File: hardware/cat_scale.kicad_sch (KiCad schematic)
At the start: 40 parts, among them J1 USB_C_Receptacle_USB2.0, J2 UART, J3 I2C, J4 LOAD CELL, J5 SSD1306, Q1 S8550, SW1 RST, SW2 BOOT, SW3 RotaryEncoder_Switch, U1 ESP32-S2-SOLO-U-N4R2, U2 AMS1117-3.3, U3 HX711

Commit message: Fixed PCB design
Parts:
- removed Q1: S8550, Package_TO_SOT_SMD:SOT-23, symbol Transistor_BJT:S8550
- added J6: Conn_01x02_Pin, Connector_PinHeader_2.54mm:PinHeader_1x02_P2.54mm_Vertical, symbol Connector:Conn_01x02_Pin
- added Q2: MMBT4403, Package_TO_SOT_SMD:SOT-23, symbol Transistor_BJT:MMBT3906
- added R11, R12: 10k, Resistor_SMD:R_1206_3216Metric, symbol Device:R
- C8: value 1uF -> 10uF
- C9: value 1uF -> 0.1uF
- D1: value LED -> PWR
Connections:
- net +3V3: now also Q2.2 (E), R11.2, R12.2; no longer J5.1 (Pin_1)
- net AVDD: now also Q2.3 (C)
- net GND: now also J6.2 (Pin_2)
- net SCL: now also J3.3 (Pin_3), J5.3 (Pin_3), U1.34 (IO41), R11.1; no longer J3.4 (Pin_4), J5.4 (Pin_4), U1.24 (IO33)
- net SDA: now also J3.4 (Pin_4), J5.4 (Pin_4), U1.35 (IO42), R12.1; no longer J3.3 (Pin_3), J5.3 (Pin_3), U1.25 (IO34)
- net +5V: now reaches C5.2, D2.1 (K), U2.3 (VI)
- net +5V: now also J5.1 (Pin_1), J6.1 (Pin_1)
- net at U3.2 (BASE): now also Q2.1 (B)
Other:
- moved on the sheet: C10, C7, C8, C9, H1, H2, H3, H4, J4, J5, R7, R8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

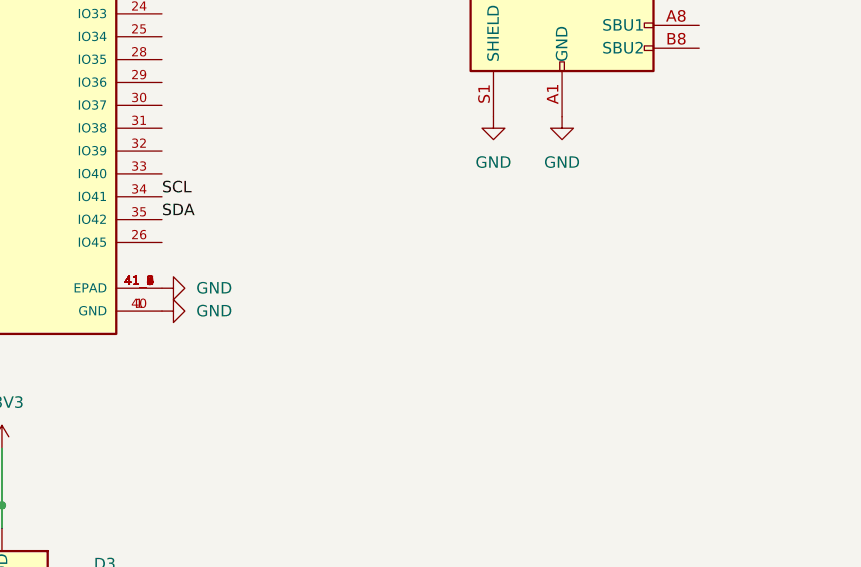
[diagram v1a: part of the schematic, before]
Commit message: * PCB: Added buzzer
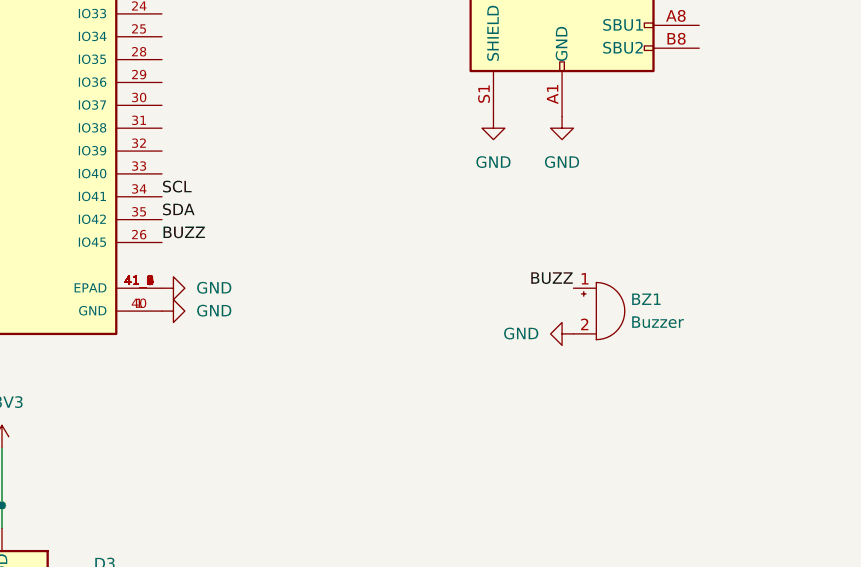
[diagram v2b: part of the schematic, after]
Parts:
- added BZ1: Buzzer, Buzzer_Beeper:Buzzer_Murata_PKMCS0909E, symbol Device:Buzzer
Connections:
- net GND: now also BZ1.2 (+)
- net BUZZ: now reaches U1.26 (IO45)
- net BUZZ: now also BZ1.1 (-)
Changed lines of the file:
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@@
+    (effects (font (size 1.27 1.27)) (justify right bottom))
+  )
+  (label "BUZZ" (at 199.39 121.92 180) (fields_autoplaced)
     (effects (font (size 1.27 1.27)) (justify right bottom))
   )
@@
   )
   (label "HX711_DATA" (at 92.71 158.75 0) (fields_autoplaced)
+    (effects (font (size 1.27 1.27)) (justify left bottom))
+  )
+  (label "BUZZ" (at 153.67 116.84 0) (fields_autoplaced)
     (effects (font (size 1.27 1.27)) (justify left bottom))
   )
@@
     )
   )
+  (symbol (lib_id "Device:Buzzer") (at 201.93 124.46 0) (unit 1)
+    (in_bom yes) (on_board yes) (dnp no) (fields_autoplaced)
+    (property "Reference" "BZ1" (at 205.74 123.19 0)
+      (effects (font (size 1.27 1.27)) (justify left))
+    )
+    (property "Value" "Buzzer" (at 205.74 125.73 0)
+      (effects (font (size 1.27 1.27)) (justify left))
+    )
+    (property "Footprint" "Buzzer_Beeper:Buzzer_Murata_PKMCS0909E" (at 201.295 121.92 90)
+      (effects (font (size 1.27 1.27)) hide)
+    )
+    (property "Datasheet" "~" (at 201.295 121.92 90)
+      (effects (font (size 1.27 1.27)) hide)
+    )
+    (pin "1")
+    (pin "2")
+    (instances
+      (project "cat_scale"
+        (path "/9f7cab82-11b1-4e5e-8a77-cae0f9a78a18"
+          (reference "BZ1") (unit 1)
+        )
+      )
+    )
+  )
   (symbol (lib_id "Device:C_Small") (at 95.25 59.69 180) (unit 1)
     (in_bom yes) (on_board yes) (dnp no) (fields_autoplaced)
@@
   )
   (symbol (lib_id "power:GND") (at 250.19 35.56 0) (unit 1)
-    (in_bom yes) (on_board yes) (dnp no) (fields_autoplaced)
+    (in_bom yes) (on_board yes) (dnp no)
     (property "Reference" "#PWR011" (at 250.19 41.91 0)
       (effects (font (size 1.27 1.27)) hide)
@@
         )
       )
+    )
+  )
+  (symbol (lib_id "power:GND") (at 199.39 127 270) (unit 1)
+    (in_bom yes) (on_board yes) (dnp no) (fields_autoplaced)
+    (property "Reference" "#PWR042" (at 193.04 127 0)
+      (effects (font (size 1.27 1.27)) hide)
+    )
+    (property "Value" "GND" (at 195.58 127 90)
+      (effects (font (size 1.27 1.27)) (justify right))
+    )
+    (property "Footprint" "" (at 199.39 127 0)
+      (effects (font (size 1.27 1.27)) hide)
+    )
+    (property "Datasheet" "" (at 199.39 127 0)
+      (effects (font (size 1.27 1.27)) hide)
+    )
+    (pin "1")
+    (instances
+      (project "cat_scale"
+        (path "/9f7cab82-11b1-4e5e-8a77-cae0f9a78a18"
+          (reference "#PWR042") (unit 1)
+        )
+      )

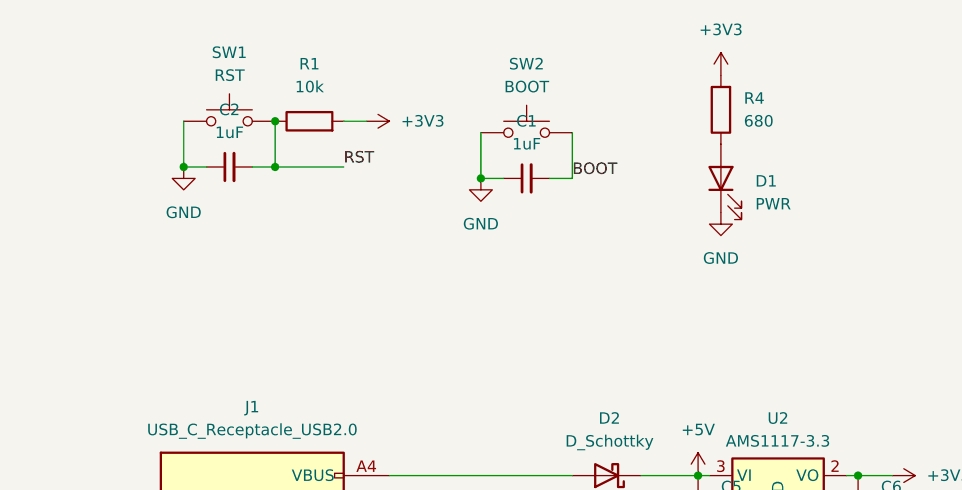
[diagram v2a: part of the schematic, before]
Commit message: Updated PCB and README
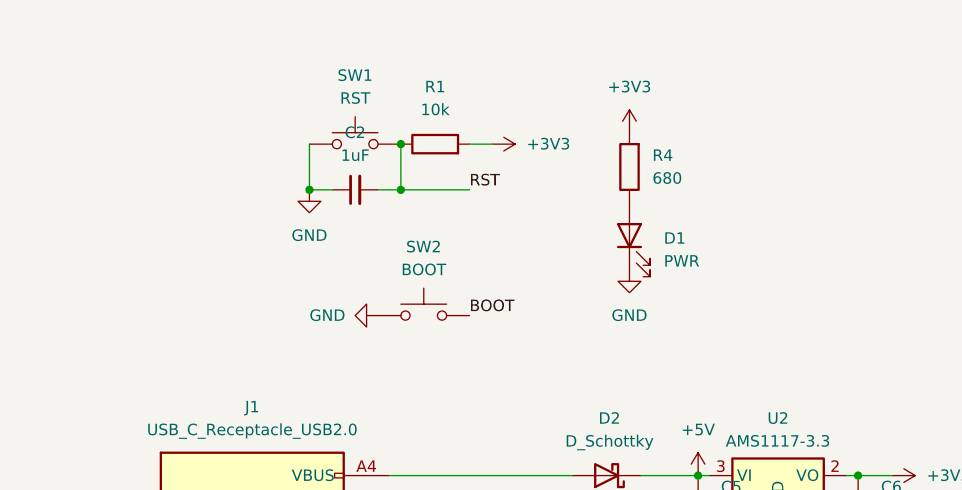
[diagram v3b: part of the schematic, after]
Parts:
- removed C1: 1uF, Capacitor_SMD:C_1206_3216Metric, symbol Device:C_Small
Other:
- moved on the sheet: C2, D1, R1, R4, SW1, SW2
